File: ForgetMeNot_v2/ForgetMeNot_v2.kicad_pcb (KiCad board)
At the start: 4 copper layers, 16 x 33 mm, 29 parts, among them J1 ISP Connector, SW1 SW_Push, U1 ATmega328PB-M, U4 LIS2HH12, U5 MCP1640x-xMC

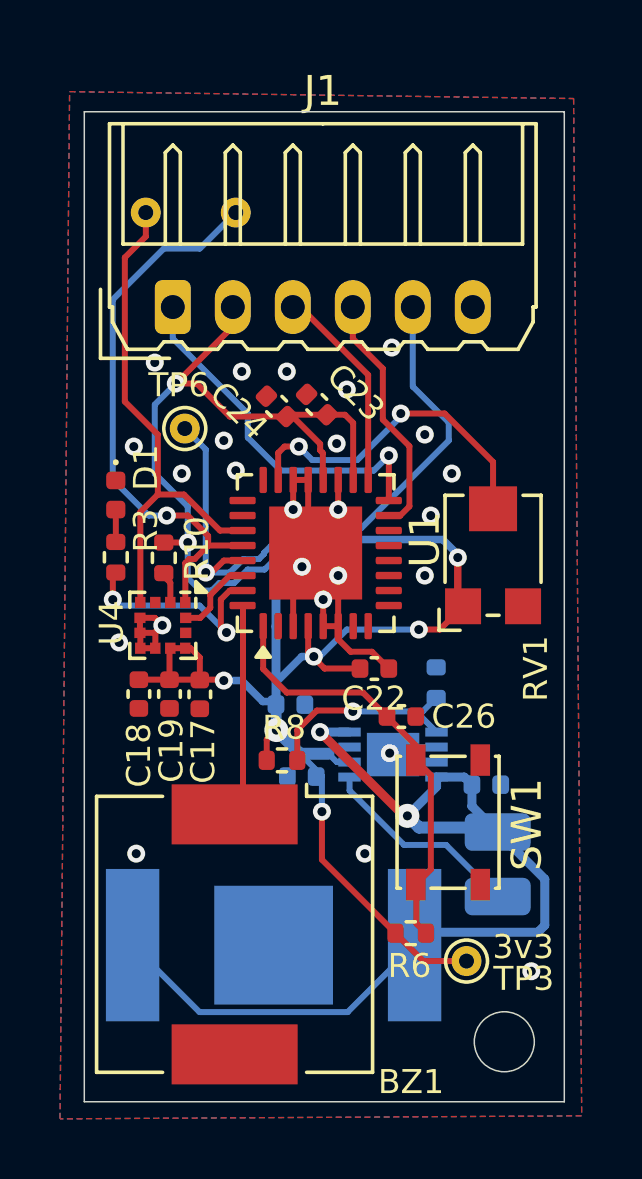
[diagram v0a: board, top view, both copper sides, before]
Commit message: swapped connector for solder pads
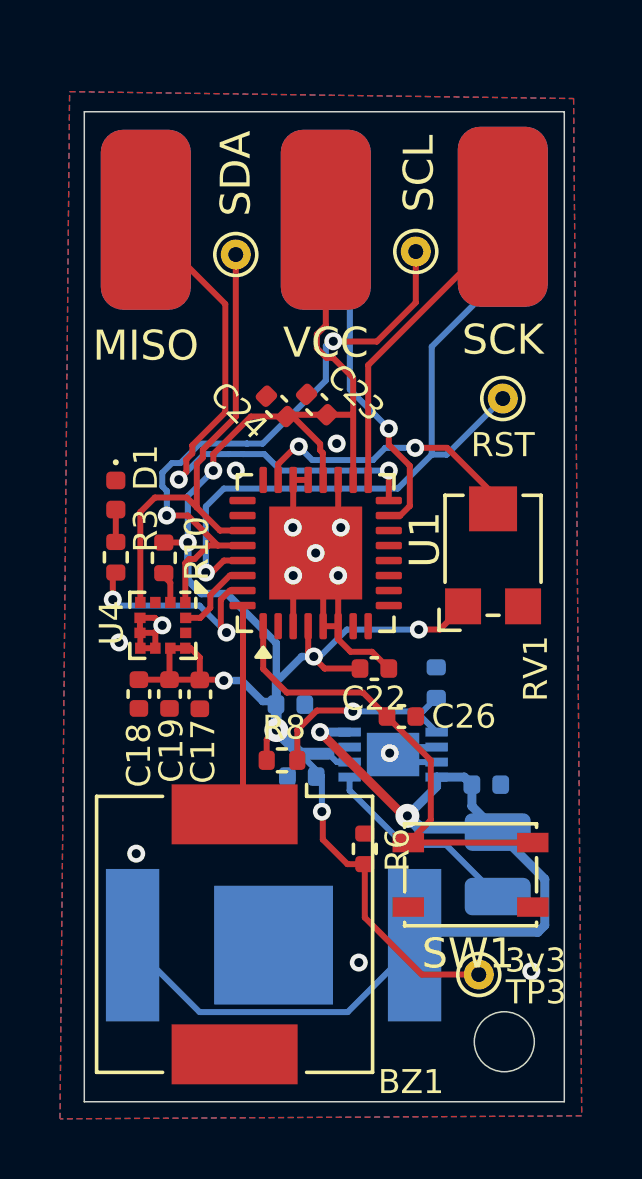
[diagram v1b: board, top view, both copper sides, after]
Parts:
- removed J1: ISP Connector, Connector_Molex:Molex_Micro-Latch_53254-0670_1x06_P2.00mm_Horizontal
- added J2: MISO, Connector_Wire:SolderWirePad_1x01_SMD_3x6mm, F.Cu at (132.7, 81.8)
- added J3: VCC, Connector_Wire:SolderWirePad_1x01_SMD_3x6mm, F.Cu at (138.7, 81.8)
- added J4: SCK, Connector_Wire:SolderWirePad_1x01_SMD_3x6mm, F.Cu at (144.6, 81.7)
- added J5: MOSI, Connector_Wire:SolderWirePad_1x01_SMD_3x6mm, B.Cu at (138.7, 81.8)
- added J6: RST, Connector_Wire:SolderWirePad_1x01_SMD_3x6mm, B.Cu at (144.6, 81.7)
- added J7: GND, Connector_Wire:SolderWirePad_1x01_SMD_3x6mm, B.Cu at (132.7, 81.8)
- TP4, TP5: moved to F.Cu
- moved TP6 10.6 mm to (144.6, 87.8)
- moved TP5 6.14 mm to (141.7, 82.9), turned to 90 degrees
- moved TP4 3.31 mm to (135.7, 83.0), turned to 0 degrees
- moved R6 3.20 mm to (140.0, 102.8), turned to 90 degrees
- moved SW1 1.90 mm to (143.5, 103.7), turned to 0 degrees
- moved TP3 0.61 mm to (143.8, 107.0)
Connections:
- U1 pad 19: GND -> (no net)
- U1 pad 22: GND -> (no net)
- U1 pad 6: GND -> VCC
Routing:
- net GND: track 27.0 -> 17.2 mm, vias 25 -> 13
- net VCC: track 75.2 -> 67.1 mm, vias 8 -> 7
- net MISO: track 12.2 -> 20.0 mm, vias 1 -> 2
- net SCK: track 6.95 -> 10.6 mm
- net MOSI: track 8.24 -> 11.8 mm, vias 0 -> 1
- net RESET: track 21.8 -> 24.1 mm
- net POT: track 11.3 -> 9.42 mm
- net ACC_SDA: track 17.6 -> 16.1 mm
- net ACC_SCL: track 19.0 -> 20.3 mm, vias 1 -> 2
- net ZERO: track 14.4 -> 15.5 mm
